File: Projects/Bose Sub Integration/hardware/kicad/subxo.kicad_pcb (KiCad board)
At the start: 2 copper layers, 101 x 104 mm, 44 parts, among them J1 IN L, J2 IN R, J3 OUT 3.5mm, J4 PWR IN 15V, J5 POLARITY SW, J6 LEVEL POT 10k, J7 INV LED, U1 TL074, U2 LM7812

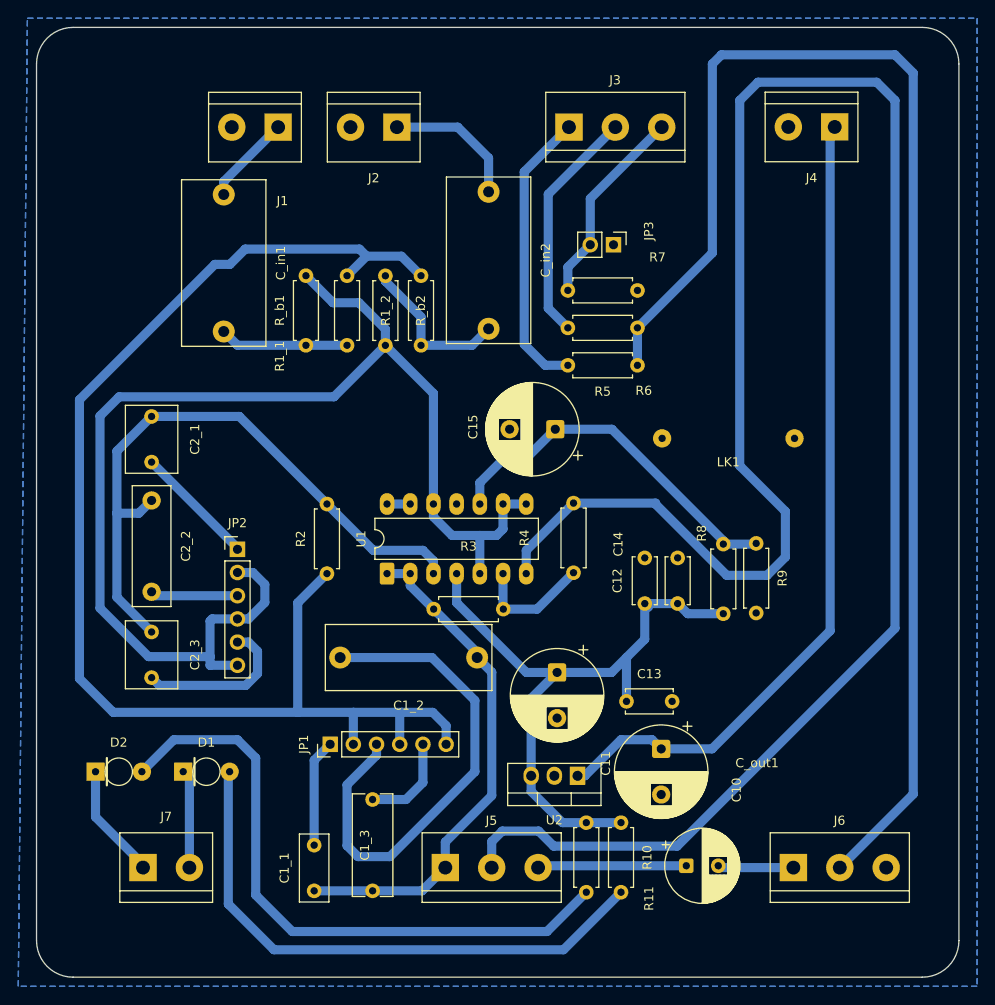
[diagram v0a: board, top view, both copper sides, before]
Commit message: Sub crossover: route rev B and export production Gerbers
214 tracks, all on B.Cu, zero vias -- still genuinely single-sided. Both ground
zones fill as one island each now, so the LK1 wire link did its job and DRC
reports zero unconnected items.

Fabrication numbers for the mill:

  board      101.0 x 104.0 mm
  clearance  0.85 mm
  track      1.00 mm
  drills     0.80, 1.00, 1.10, 1.20, 1.52 mm, no NPTH
  layers     B_Cu + Edge_Cuts only

CUT THIS WITH A 0.4 mm (1/64") ENDMILL. At 0.85 mm clearance a 0.8 mm bit
cannot isolate the channels -- that would need a rebuild at 1.2 mm.

Six DRC warnings remain and all are cosmetic. C11's reference designator sits on
U2's outline with nowhere to go, and D1/D2 report a library mismatch because the
board carries the earlier 1.5 mm LED silk circle rather than the 1.2 mm one. That
difference is silkscreen only; the copper and drill are correct, and the LED pads
are on the 5.08 mm pitch as intended.

Note the three DXF exports under production/ are still from 14 August and
describe rev A. They are for the laser, not the mill, so nothing in this run
uses them -- but do not feed them to anything until they are regenerated.
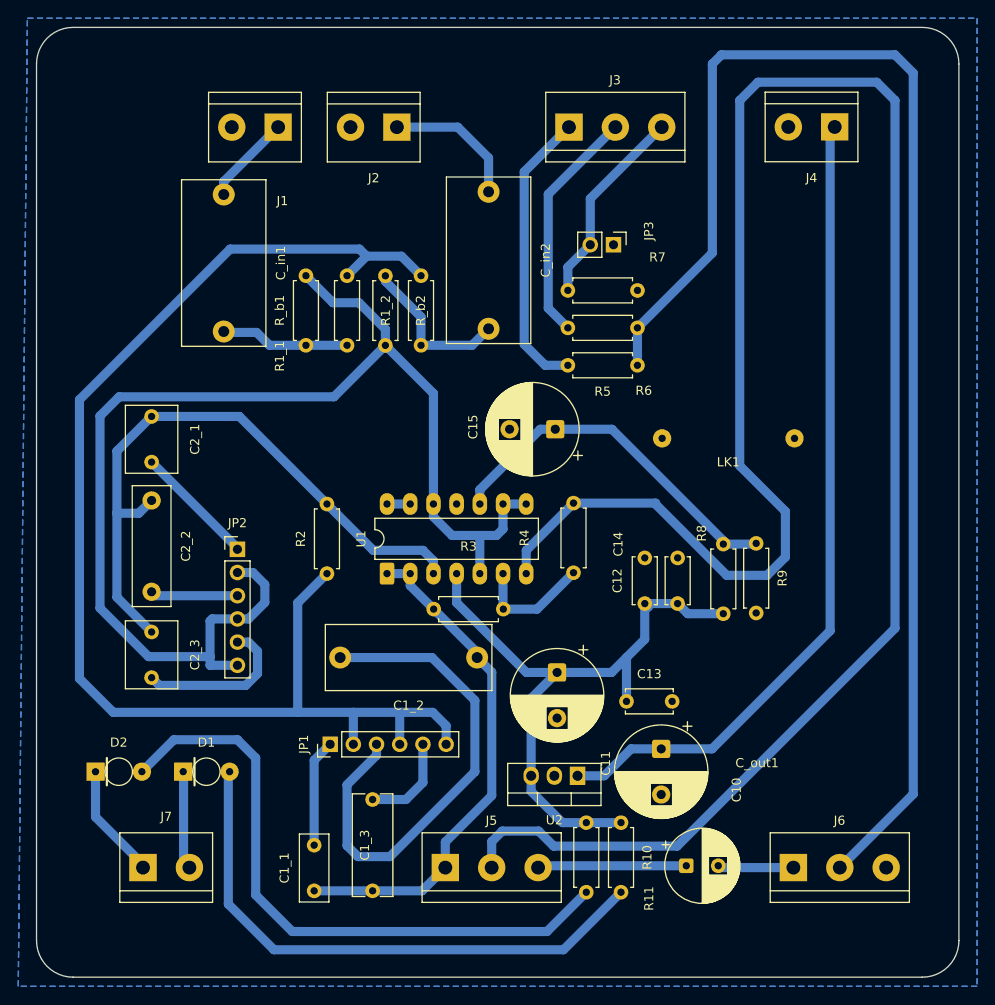
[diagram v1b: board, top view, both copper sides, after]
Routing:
- net /VIN: track 90.4 -> 89.6 mm
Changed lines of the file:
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@@
-	)
-	(segment
-		(start 150.4 114)
-		(end 151.4 115)
-		(width 1)
-		(layer "B.Cu")
-		(net "/VIN")
 	)
 	(segment
@@
 	)
 	(segment
-		(start 147 114)
-		(end 150.4 114)
+		(start 148.1 115)
+		(end 151.4 115)
 		(width 1)
 		(layer "B.Cu")
@@
 	)
 	(segment
-		(start 143.05 117.95)
-		(end 147 114)
+		(start 142.24 117.95)
+		(end 145.15 117.95)
 		(width 1)
 		(layer "B.Cu")
@@
 	)
 	(segment
-		(start 142.24 117.95)
-		(end 143.05 117.95)
+		(start 145.15 117.95)
+		(end 148.1 115)
 		(width 1)
 		(layer "B.Cu")
@@
 	)
 	(segment
+		(start 99.1 127.36)
+		(end 99.1 117.54)
+		(width 1)
+		(layer "B.Cu")
+		(net "/GND")
+	)
+	(segment
 		(start 99.74 128)
-		(end 99.74 118.18)
+		(end 99.1 127.36)
 		(width 1)
 		(layer "B.Cu")
@@
 	)
 	(segment
-		(start 99.74 118.18)
+		(start 99.1 117.54)
 		(end 99.06 117.5)
 		(width 1)
@@
 	)
 	(segment
+		(start 131.54 86.625)
+		(end 138.165 80)
+		(width 1)
+		(layer "B.Cu")
+		(net "/VG_DIV")
+	)
+	(segment
 		(start 139.8 80)
 		(end 146 80)
@@
 	)
 	(segment
-		(start 131.54 85.86)
-		(end 134.5 82.9)
-		(width 1)
-		(layer "B.Cu")
-		(net "/VG_DIV")
-	)
-	(segment
-		(start 134.5 82.9)
-		(end 136.9 82.9)
-		(width 1)
-		(layer "B.Cu")
-		(net "/VG_DIV")
-	)
-	(segment
 		(start 131.54 88.19)
-		(end 131.54 85.86)
+		(end 131.54 86.625)
 		(width 1)
 		(layer "B.Cu")
@@
 	)
 	(segment
-		(start 136.9 82.9)
+		(start 138.165 80)
 		(end 139.8 80)
 		(width 1)
@@
 	)
 	(segment
-		(start 104.173402 61.95)
-		(end 102.526598 61.95)
-		(width 1)
-		(layer "B.Cu")
-		(net "/N1")
-	)
-	(segment
 		(start 122.77 114.5)
 		(end 122.77 111.23)
@@
 	)
 	(segment
-		(start 118.363402 60.273402)
-		(end 105.85 60.273402)
-		(width 1)
-		(layer "B.Cu")
-		(net "/N1")
-	)
-	(segment
-		(start 105.85 60.273402)
-		(end 104.173402 61.95)
+		(start 87.7 76.776598)
+		(end 87.7 107.3)
+		(width 1)
+		(layer "B.Cu")
+		(net "/N1")
+	)
+	(segment
+		(start 104.203196 60.273402)
+		(end 87.7 76.776598)
+		(width 1)
+		(layer "B.Cu")
+		(net "/N1")
+	)
+	(segment
+		(start 111.6 99.01)
+		(end 111.6 111)
 		(width 1)
 		(layer "B.Cu")
@@
 	)
 	(segment
-		(start 111.6 99.01)
-		(end 111.6 111)
-		(width 1)
-		(layer "B.Cu")
-		(net "/N1")
-	)
-	(segment
 		(start 117.69 114.5)
 		(end 117.69 111.01)
@@
 	)
 	(segment
+		(start 127.85 114.5)
+		(end 127.85 112.466296)
+		(width 1)
+		(layer "B.Cu")
+		(net "/N1")
+	)
+	(segment
+		(start 122.77 111.23)
+		(end 123 111)
+		(width 1)
+		(layer "B.Cu")
+		(net "/N1")
+	)
+	(segment
+		(start 117.7 111)
+		(end 111.6 111)
+		(width 1)
+		(layer "B.Cu")
+		(net "/N1")
+	)
+	(segment
+		(start 127.85 112.466296)
+		(end 126.383704 111)
+		(width 1)
+		(layer "B.Cu")
+		(net "/N1")
+	)
+	(segment
+		(start 91.4 111)
+		(end 111.6 111)
+		(width 1)
+		(layer "B.Cu")
+		(net "/N1")
+	)
+	(segment
 		(start 87.7 107.3)
 		(end 91.4 111)
@@
 	)
 	(segment
-		(start 127.85 114.5)
-		(end 127.85 112.466296)
-		(width 1)
-		(layer "B.Cu")
-		(net "/N1")
-	)
-	(segment
-		(start 87.7 76.776598)
-		(end 87.7 107.3)
-		(width 1)
-		(layer "B.Cu")
-		(net "/N1")
-	)
-	(segment
-		(start 122.77 111.23)
-		(end 123 111)
-		(width 1)
-		(layer "B.Cu")
-		(net "/N1")
-	)
-	(segment
-		(start 117.7 111)
-		(end 111.6 111)
-		(width 1)
-		(layer "B.Cu")
-		(net "/N1")
-	)
-	(segment
-		(start 127.85 112.466296)
-		(end 126.383704 111)
-		(width 1)
-		(layer "B.Cu")
-		(net "/N1")
-	)
-	(segment
-		(start 91.4 111)
-		(end 111.6 111)
-		(width 1)
-		(layer "B.Cu")
-		(net "/N1")
-	)
-	(segment
-		(start 102.526598 61.95)
-		(end 87.7 76.776598)
+		(start 118.363402 60.273402)
+		(end 104.203196 60.273402)
 		(width 1)
 		(layer "B.Cu")
@@
 	)
 	(segment
-		(start 112.5 70.81)
-		(end 105.01 70.81)
-		(width 1)
-		(layer "B.Cu")
-		(net "/A_L")
-	)
-	(segment
 		(start 117 70.81)
 		(end 112.5 70.81)
@@
 	)
 	(segment
-		(start 105.01 70.81)
+		(start 103.6 69.4)
 		(end 103.5 69.3)
 		(width 1)
 		(layer "B.Cu")
+		(net "/A_L")
+	)
+	(segment
+		(start 112.5 70.81)
+		(end 108.51 70.81)
+		(width 1)
+		(layer "B.Cu")
+		(net "/A_L")
+	)
+	(segment
+		(start 108.51 70.81)
+		(end 107.1 69.4)
+		(width 1)
+		(layer "B.Cu")
+		(net "/A_L")
+	)
+	(segment
+		(start 107.1 69.4)
+		(end 103.6 69.4)
+		(width 1)
+		(layer "B.Cu")
